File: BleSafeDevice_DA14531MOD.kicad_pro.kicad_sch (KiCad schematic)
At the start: 20 parts, among them J1 SWD_DEBUG_PADS, J2 CURRENT_MEAS_PADS, SW1 PTS526SK15SMTR2 LFS, U4 DA14531MOD-00F01002

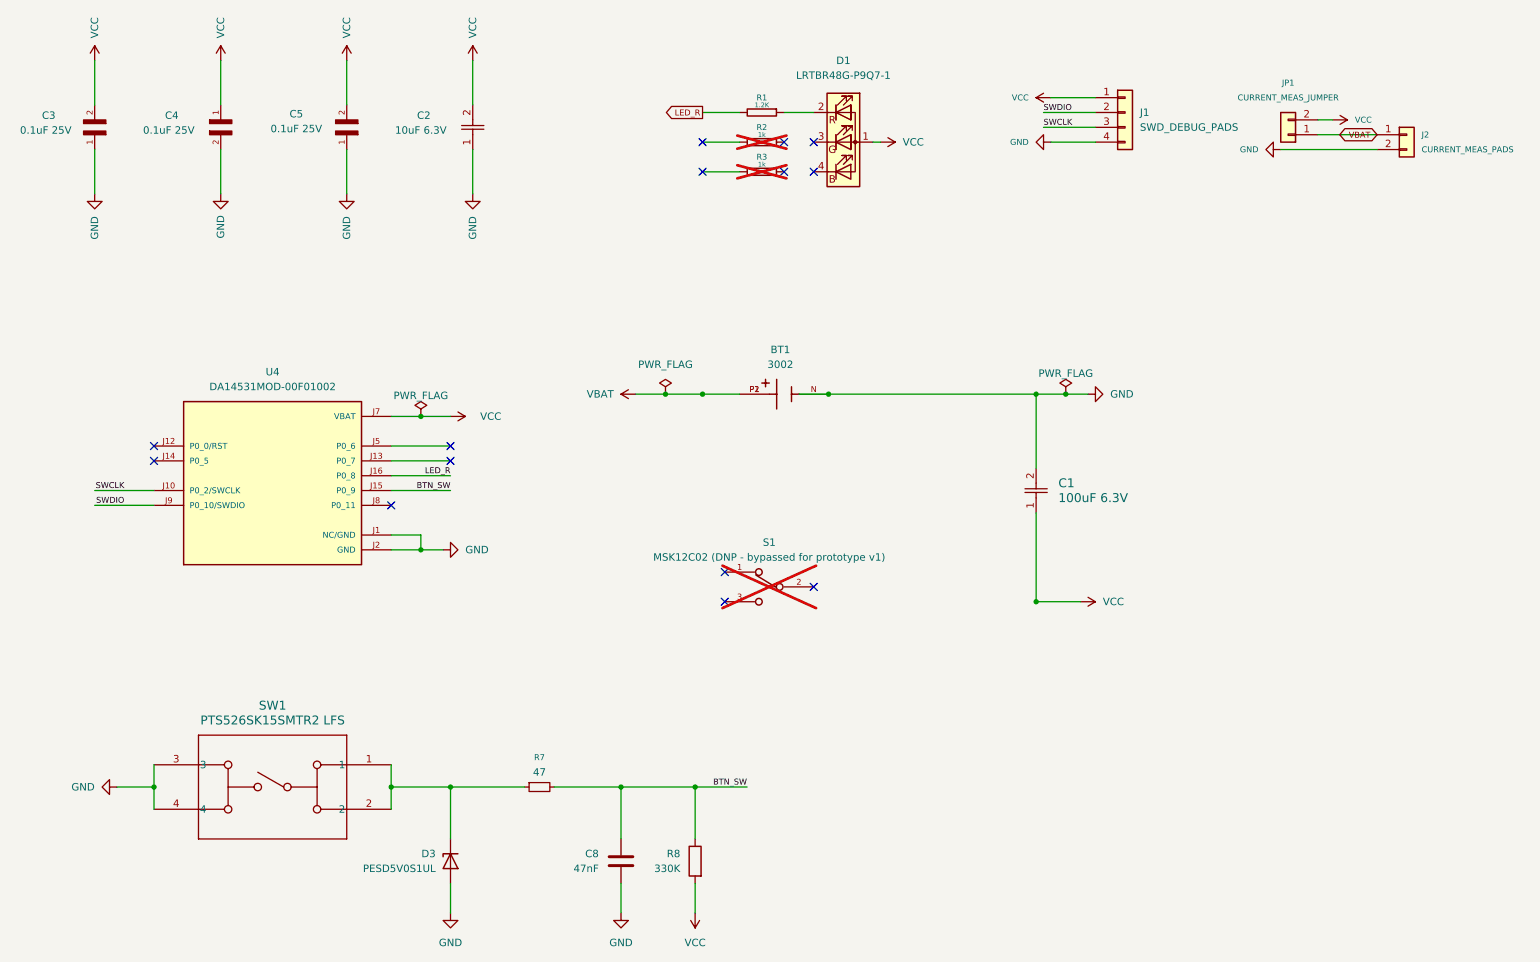
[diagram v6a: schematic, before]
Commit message: Replace RGB LED with JLC-friendly red 0603 LED
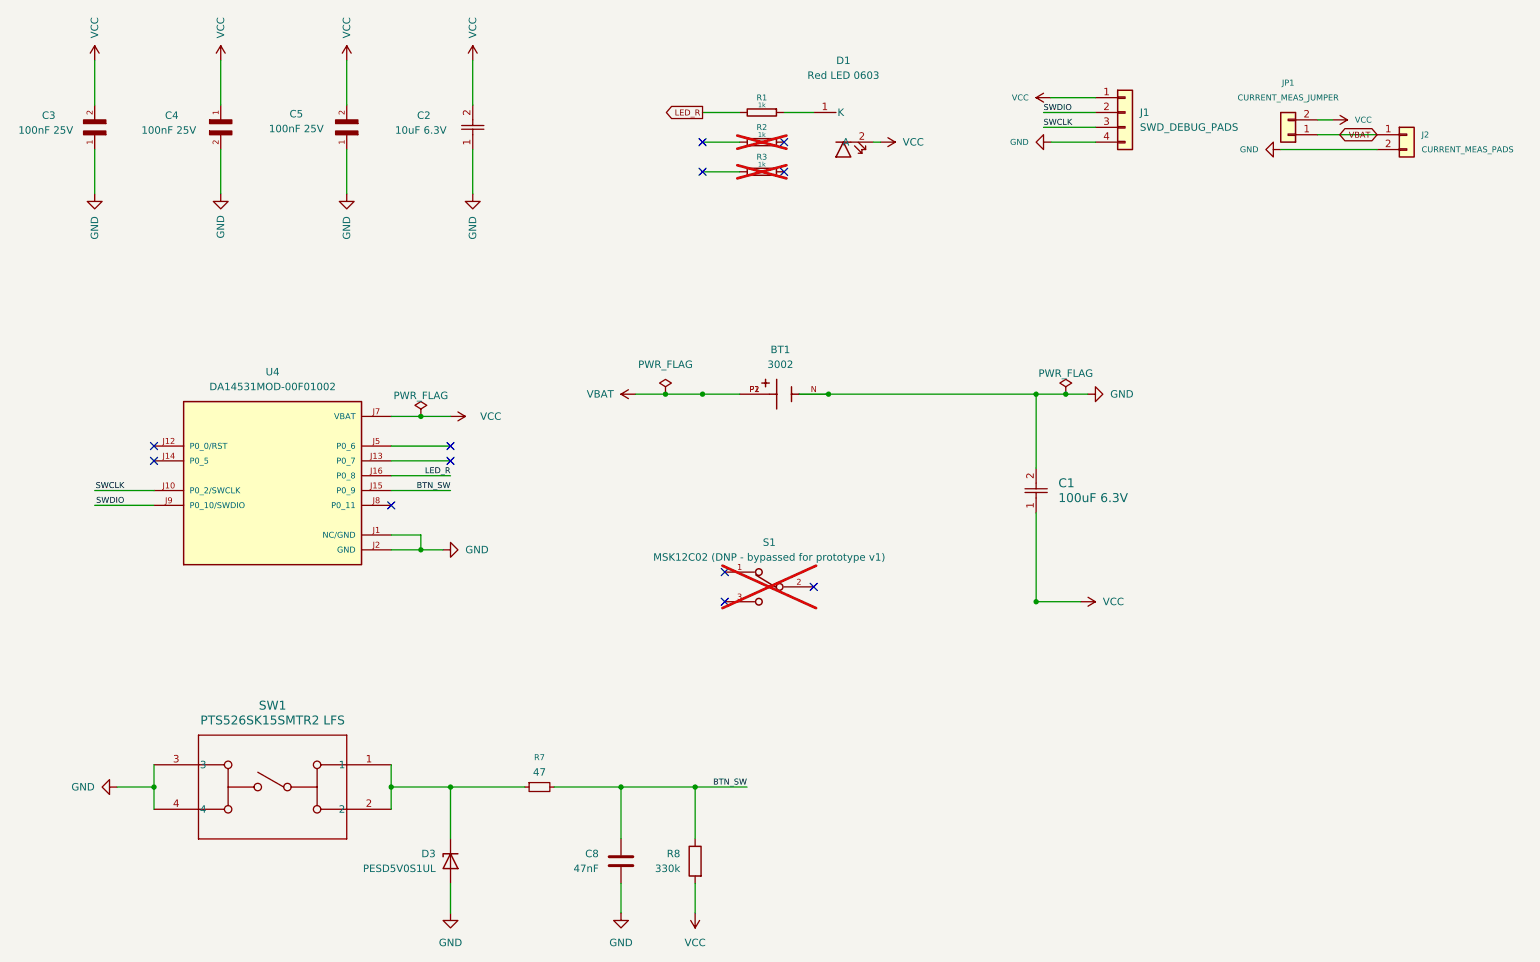
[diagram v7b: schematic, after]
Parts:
- C3, C4, C5: value 0.1uF 25V -> 100nF 25V; MPN CL05A104KA5NNNC -> (none); Manufacturer (none) -> Generic
- D1: value LRTBR48G-P9Q7-1 -> Red LED 0603; footprint SafeGuardPing_Local:LED_RGB_amsOSRAM_LRTBR48G -> SafeGuardPing_Local:LED_0603_1608Metric_Red_Generic; symbol Device:LED_ARGB -> SafeGuardPing_Local:LED_Red_0603_Generic; MPN LRTBR48G-P9Q7-1+R7S5-26+NP-68 -> (none); Manufacturer (none) -> Generic
- J1, J2, JP1: now left out of the parts list
- R1: value 1.2K -> 1k; Manufacturer (none) -> Generic
- R7: Manufacturer (none) -> Generic
- R8: value 330K -> 330k; Manufacturer (none) -> Generic
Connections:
- net VCC: now also D1.2 (A); no longer D1.1 (A)
- net at R1.1: now also D1.1 (K); no longer D1.2 (RK)
- no-connect marks 14 -> 12
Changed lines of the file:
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@@
 	)
 	(no_connect
-		(at 156.21 39.37)
-	)
-	(no_connect
-		(at 156.21 44.45)
-	)
-	(no_connect
 		(at 151.13 39.37)
 	)
@@
 			)
 		)
-		(property "Value" "1.2K"
+		(property "Value" "1k"
 			(at 147.32 33.02 90)
 			(effects
@@
 			)
 		)
+		(property "MPN" ""
+			(at 0 0 0)
+			(effects
+				(font
+					(size 1.27 1.27)
+				)
+				(hide yes)
+			)
+		)
+		(property "Manufacturer" "Generic"
+			(at 0 0 0)
+			(effects
+				(font
+					(size 1.27 1.27)
+				)
+				(hide yes)
+			)
+		)
 		(pin "1"
 		)
@@
 			)
 		)
-		(property "Value" "0.1uF 25V"
+		(property "Value" "100nF 25V"
 			(at 67.564 37.084 90)
 			(effects
@@
 			)
 		)
-		(property "MPN" "CL05A104KA5NNNC"
+		(property "MPN" ""
 			(at 76.2 38.1 0)
 			(effects
@@
 			)
 		)
+		(property "Manufacturer" "Generic"
+			(at 0 0 0)
+			(effects
+				(font
+					(size 1.27 1.27)
+				)
+				(hide yes)
+			)
+		)
 		(pin "2"
 		)
@@
 			)
 		)
-		(property "Value" "330K"
+		(property "Value" "330k"
 			(at 133.35 163.8299 0)
 			(effects
@@
 			)
 		)
+		(property "MPN" ""
+			(at 0 0 0)
+			(effects
+				(font
+					(size 1.27 1.27)
+				)
+				(hide yes)
+			)
+		)
+		(property "Manufacturer" "Generic"
+			(at 0 0 0)
+			(effects
+				(font
+					(size 1.27 1.27)
+				)
+				(hide yes)
+			)
+		)
 		(pin "1"
 		)
@@
 		(unit 1)
 		(exclude_from_sim no)
-		(in_bom yes)
+		(in_bom no)
 		(on_board yes)
 		(dnp no)
@@
 			)
 		)
+		(property "MPN" ""
+			(at 0 0 0)
+			(effects
+				(font
+					(size 1.27 1.27)
+				)
+				(hide yes)
+			)
+		)
+		(property "Manufacturer" ""
+			(at 0 0 0)
+			(effects
+				(font
+					(size 1.27 1.27)
+				)
+				(hide yes)
+			)
+		)
 		(pin "1"
 		)
@@
 		(unit 1)
 		(exclude_from_sim no)
-		(in_bom yes)
+		(in_bom no)
 		(on_board yes)
 		(dnp no)
@@
 			)
 		)
+		(property "MPN" ""
+			(at 0 0 0)
+			(effects
+				(font
+					(size 1.27 1.27)
+				)
+				(hide yes)
+			)
+		)
+		(property "Manufacturer" ""
+			(at 0 0 0)
+			(effects
+				(font
+					(size 1.27 1.27)
+				)
+				(hide yes)
+			)
+		)
 		(pin "2"
 		)
@@
 			)
 		)
-		(property "Value" "0.1uF 25V"
+		(property "Value" "100nF 25V"
 			(at 24.638 37.338 90)
 			(effects
@@
 			)
 		)
-		(property "MPN" "CL05A104KA5NNNC"
+		(property "MPN" ""
 			(at 33.02 38.1 0)
 			(effects
@@
 			)
 		)
+		(property "Manufacturer" "Generic"
+			(at 0 0 0)
+			(effects
+				(font
+					(size 1.27 1.27)
+				)
+				(hide yes)
+			)
+		)
 		(pin "2"
 		)
@@
 		(unit 1)
 		(exclude_from_sim no)
-		(in_bom yes)
+		(in_bom no)
 		(on_board yes)
 		(dnp no)
@@
 			)
 		)
+		(property "MPN" ""
+			(at 0 0 0)
+			(effects
+				(font
+					(size 1.27 1.27)
+				)
+				(hide yes)
+			)
+		)
+		(property "Manufacturer" ""
+			(at 0 0 0)
+			(effects
+				(font
+					(size 1.27 1.27)
+				)
+				(hide yes)
+			)
+		)
 		(pin "2"
 		)
@@
 			)
 		)
+		(property "MPN" ""
+			(at 0 0 0)
+			(effects
+				(font
+					(size 1.27 1.27)
+				)
+				(hide yes)
+			)
+		)
+		(property "Manufacturer" "Generic"
+			(at 0 0 0)
+			(effects
+				(font
+					(size 1.27 1.27)
+				)
+				(hide yes)
+			)
+		)
 		(pin "1"
 		)
@@
 	)
 	(symbol
-		(lib_id "Device:LED_ARGB")
+		(lib_id "SafeGuardPing_Local:LED_Red_0603_Generic")
 		(at 161.29 39.37 0)
 		(unit 1)
@@
 			)
 		)
-		(property "Value" "LRTBR48G-P9Q7-1"
+		(property "Value" "Red LED 0603"
 			(at 161.29 27.94 0)
 			(effects
@@
 			)
 		)
-		(property "Footprint" "SafeGuardPing_Local:LED_RGB_amsOSRAM_LRTBR48G"
+		(property "Footprint" "SafeGuardPing_Local:LED_0603_1608Metric_Red_Generic"
 			(at 161.29 40.64 0)
 			(effects
@@
 			)
 		)
-		(property "Datasheet" "https://www.alldatasheet.com/datasheet-pdf/pdf/1047991/OSRAM/LRTB-R48G.html"
+		(property "Datasheet" "~"
 			(at 161.29 40.64 0)
 			(effects
@@
 			)
 		)
-		(property "Description" "ams OSRAM LRTB R48G RGB LED, 1.0 mm x 1.0 mm, common anode; pin 1 A, pin 2 red K, pin 3 green K, pin 4 blue K"
+		(property "Description" "Generic red LED, 0603 / 1608 metric, prototype-v1 single red status LED"
 			(at 161.29 39.37 0)
 			(effects
@@
 			)
 		)
-		(property "MPN" "LRTBR48G-P9Q7-1+R7S5-26+NP-68"
+		(property "MPN" ""
 			(at 161.29 39.37 0)
 			(effects
@@
 			)
 		)
-		(pin "2"
-		)
-		(pin "1"
-		)
-		(pin "3"
-		)
-		(pin "4"
+		(property "Manufacturer" "Generic"
+			(at 0 0 0)
+			(effects
+				(font
+					(size 1.27 1.27)
+				)
+				(hide yes)
+			)
 		)
 		(instances
@@
 			)
 		)
-		(property "Value" "0.1uF 25V"
+		(property "Value" "100nF 25V"
 			(at 45.72 37.338 90)
 			(effects
@@
 			)
 		)
-		(property "MPN" "CL05A104KA5NNNC"
+		(property "MPN" ""
 			(at 54.61 35.56 0)
 			(effects
 				(font
+					(size 1.27 1.27)
+				)
+				(hide yes)
+			)
+		)
+		(property "Manufacturer" "Generic"
+			(at 0 0 0)
+			(effects
+				(font

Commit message: Restore production-close Ping power switch
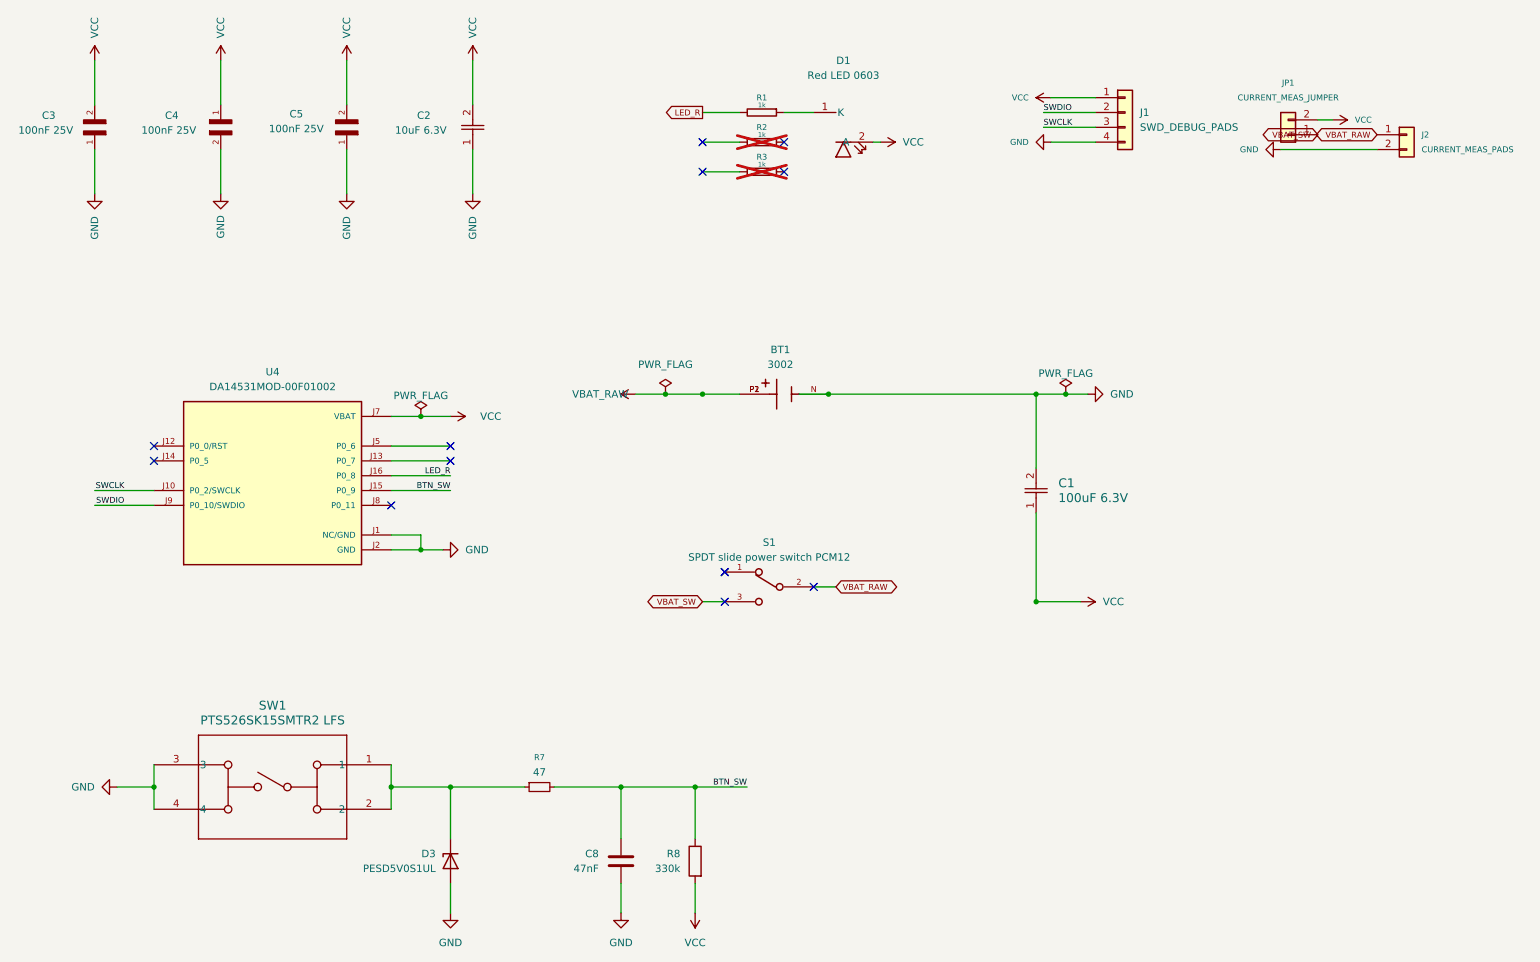
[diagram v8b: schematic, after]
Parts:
- C3, C4, C5: MF Samsung Electro-Mechanics -> Generic; MP CL05A104KA5NNNC -> (none)
- S1: value MSK12C02 (DNP - bypassed for prototype v1) -> SPDT slide power switch PCM12; Description_1 Sub-Miniature Slide Switch-DPDT-0.3A@6VDC-Surface Mount-5,0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 -> Low-profile SPDT slide switch for user ON/OFF battery power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; MANUFACTURER C&K -> Generic; MF Littelfuse/C&K -> Generic; MP JS102011SAQN -> (none); now fitted; now in the parts list
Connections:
- net VBAT_RAW: now reaches S1.2
- net VBAT_RAW: now also BT1.P1, BT1.P2, J2.1 (Pin_1)
- net VBAT_SW: now reaches S1.3
- net VBAT_SW: now also JP1.1 (Pin_1)
- removed net VBAT: BT1.P1, BT1.P2, J2.1 (Pin_1), JP1.1 (Pin_1)
- no-connect marks 12 -> 13
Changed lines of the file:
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@@
 	(wire
 		(pts
-			(xy 242.57 38.1) (xy 252.73 38.1)
-		)
-		(stroke
-			(width 0)
-			(type default)
-		)
-	)
-	(wire
-		(pts
 			(xy 135.89 149.86) (xy 135.89 158.75)
 		)
@@
 		)
 	)
-	(global_label "VBAT"
+	(global_label "VBAT_RAW"
 		(shape bidirectional)
 		(at 252.73 38.1 180)
@@
 		)
 	)
+	(global_label "VBAT_SW"
+		(shape bidirectional)
+		(at 242.57 38.1 180)
+		(fields_autoplaced yes)
+		(effects
+			(font
+				(size 1.016 1.016)
+			)
+			(justify right)
+		)
+		(property "Intersheetrefs" "${INTERSHEET_REFS}"
+			(at 235.6343 38.1 0)
+			(effects
+				(font
+					(size 1.27 1.27)
+				)
+				(justify right)
+				(hide yes)
+			)
+		)
+	)
+	(wire
+		(pts
+			(xy 140.97 118.11) (xy 137.16 118.11)
+		)
+		(stroke
+			(width 0)
+			(type default)
+		)
+	)
+	(wire
+		(pts
+			(xy 156.21 115.57) (xy 160.02 115.57)
+		)
+		(stroke
+			(width 0)
+			(type default)
+		)
+	)
+	(global_label "VBAT_SW"
+		(shape bidirectional)
+		(at 137.16 118.11 180)
+		(fields_autoplaced yes)
+		(effects
+			(font
+				(size 1.016 1.016)
+			)
+			(justify right)
+		)
+		(property "Intersheetrefs" "${INTERSHEET_REFS}"
+			(at 130.2243 118.11 0)
+			(effects
+				(font
+					(size 1.27 1.27)
+				)
+				(justify right)
+				(hide yes)
+			)
+		)
+	)
+	(global_label "VBAT_RAW"
+		(shape bidirectional)
+		(at 160.02 115.57 0)
+		(fields_autoplaced yes)
+		(effects
+			(font
+				(size 1.016 1.016)
+			)
+			(justify left)
+		)
+		(property "Intersheetrefs" "${INTERSHEET_REFS}"
+			(at 166.9557 115.57 0)
+			(effects
+				(font
+					(size 1.27 1.27)
+				)
+				(justify left)
+				(hide yes)
+			)
+		)
+	)
+	(no_connect
+		(at 140.97 113.03)
+	)
 	(symbol
 		(lib_name "R_1")
@@
 			)
 		)
-		(property "MF" "Samsung Electro-Mechanics"
+		(property "MF" "Generic"
 			(at 76.2 38.1 0)
 			(effects
@@
 			)
 		)
-		(property "MP" "CL05A104KA5NNNC"
+		(property "MP" ""
 			(at 76.2 38.1 0)
 			(effects
@@
 		(unit 1)
 		(exclude_from_sim no)
-		(in_bom no)
-		(on_board no)
-		(dnp yes)
+		(in_bom yes)
+		(on_board yes)
+		(dnp no)
 		(fields_autoplaced yes)
 		(property "Reference" "S1"
@@
 			)
 		)
-		(property "Value" "MSK12C02 (DNP - bypassed for prototype v1)"
+		(property "Value" "SPDT slide power switch PCM12"
 			(at 148.59 110.49 0)
 			(effects
@@
 			)
 		)
-		(property "MF" "Littelfuse/C&K"
+		(property "MF" "Generic"
 			(at 148.59 115.57 0)
 			(effects
@@
 			)
 		)
-		(property "Description_1" "Sub-Miniature Slide Switch-DPDT-0.3A@6VDC-Surface Mount-5,000 Cycles"
+		(property "Description_1" "Low-profile SPDT slide switch for user ON/OFF battery power, PCM12 footprint"
 			(at 148.59 115.57 0)
 			(effects
@@
 			)
 		)
-		(property "MP" "JS102011SAQN"
+		(property "MP" ""
 			(at 148.59 115.57 0)
 			(effects
@@
 			)
 		)
-		(property "MANUFACTURER" "C&K"
+		(property "MANUFACTURER" "Generic"
 			(at 148.59 115.57 0)
 			(effects
@@
 			)
 		)
-		(property "MF" "Samsung Electro-Mechanics"
+		(property "MF" "Generic"
 			(at 33.02 38.1 0)
 			(effects
@@
 			)
 		)
-		(property "MP" "CL05A104KA5NNNC"
+		(property "MP" ""
 			(at 33.02 38.1 0)
 			(effects
@@
 			)
 		)
-		(property "Value" "VBAT"
+		(property "Value" "VBAT_RAW"
 			(at 119.634 82.55 90)
 			(effects
@@
 			)
 		)
-		(property "MF" "Samsung Electro-Mechanics"
+		(property "MF" "Generic"
 			(at 54.61 35.56 0)
 			(effects
@@
 			)
 		)
-		(property "MP" "CL05A104KA5NNNC"
+		(property "MP" ""
 			(at 54.61 35.56 0)
 			(effects
